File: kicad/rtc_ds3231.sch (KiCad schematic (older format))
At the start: 10 parts, among them U6 DS3231N

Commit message: footprint corrections on PCB
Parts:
- BT1: symbol KlokTHREEjr:Batt_RTC -> wyostat:Batt_RTC; manf# (none) -> mfr_pn
- C8: symbol KlokTHREEjr:C_NP -> wyostat:C_NP; manf# (none) -> mfr_pn
- R26, R27, R28, R29: symbol KlokTHREEjr:R -> wyostat:R; manf# (none) -> mfr_pn
- TP1, TP2, TP3: symbol KlokTHREEjr:Conn_01x01 -> wyostat:Conn_01x01; manf# (none) -> mfr_pn
- U6: symbol KlokTHREEjr:DS3231N -> wyostat:DS3231N; manf# (none) -> mfr_pn
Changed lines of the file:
@@
 $EndDescr
 $Comp
-L KlokTHREEjr:R R28
+L wyostat:R R28
 U 1 1 5A448924
 P 2525 2750
@@
 F 2 "wyostat_fp:R_0805" V 2455 2750 30  0001 C CNN
 F 3 "~" H 2525 2750 30  0000 C CNN
+F 4 "mfr_pn" H 2525 2750 50  0001 C CNN "manf#"
 	1    2525 2750
 	1    0    0    -1
 $EndComp
 $Comp
-L KlokTHREEjr:GND #PWR017
+L wyostat:GND #PWR017
 U 1 1 5A44892B
 P 3675 4175
@@
 F 2 "" H 3675 4175 60  0000 C CNN
 F 3 "" H 3675 4175 60  0000 C CNN
+F 4 "mfr_pn" H 3675 4175 50  0001 C CNN "manf#"
 	1    3675 4175
 	1    0    0    -1
 $EndComp
 $Comp
-L KlokTHREEjr:R R26
+L wyostat:R R26
 U 1 1 5A448933
 P 4900 2550
@@
 F 2 "wyostat_fp:R_0805" V 4830 2550 30  0001 C CNN
 F 3 "~" H 4900 2550 30  0000 C CNN
+F 4 "mfr_pn" H 4900 2550 50  0001 C CNN "manf#"
 	1    4900 2550
 	1    0    0    -1
 $EndComp
 $Comp
-L KlokTHREEjr:R R27
+L wyostat:R R27
 U 1 1 5A44893A
 P 5050 2550
@@
 F 2 "wyostat_fp:R_0805" V 4980 2550 30  0001 C CNN
 F 3 "~" H 5050 2550 30  0000 C CNN
+F 4 "mfr_pn" H 5050 2550 50  0001 C CNN "manf#"
 	1    5050 2550
 	1    0    0    -1
@@
 RESET
 $Comp
-L KlokTHREEjr:PWR_FLAG #FLG018
+L wyostat:PWR_FLAG #FLG018
 U 1 1 5A448942
 P 2000 2325
@@
 F 2 "" H 2000 2325 60  0000 C CNN
 F 3 "" H 2000 2325 60  0000 C CNN
+F 4 "mfr_pn" H 2000 2325 50  0001 C CNN "manf#"
 	1    2000 2325
 	1    0    0    -1
 $EndComp
 $Comp
-L KlokTHREEjr:DS3231N U6
+L wyostat:DS3231N U6
 U 1 1 5A448948
 P 3675 3200
@@
 F 2 "wyostat_fp:DS3231" H 3675 3200 60  0001 C CNN
 F 3 "~" H 3675 3200 60  0000 C CNN
+F 4 "mfr_pn" H 3675 3200 50  0001 C CNN "manf#"
 	1    3675 3200
 	1    0    0    -1
 $EndComp
 $Comp
-L KlokTHREEjr:R R29
+L wyostat:R R29
 U 1 1 5A44894F
 P 2675 2750
@@
 F 2 "wyostat_fp:R_0805" V 2605 2750 30  0001 C CNN
 F 3 "~" H 2675 2750 30  0000 C CNN
+F 4 "mfr_pn" H 2675 2750 50  0001 C CNN "manf#"
 	1    2675 2750
 	1    0    0    -1
 $EndComp
 $Comp
-L KlokTHREEjr:Batt_RTC BT1
+L wyostat:Batt_RTC BT1
 U 1 1 5A448957
 P 2000 3200
@@
 F 2 "wyostat_fp:CR2032_SMD2" H 2000 3200 60  0001 C CNN
 F 3 "" H 2000 3200 60  0000 C CNN
-F 4 "BU2032SM-HD-GCT-ND " H 2100 3500 60  0001 C CNN "Digikey"
+F 4 "mfr_pn" H 2000 3200 50  0001 C CNN "manf#"
+F 5 "BU2032SM-HD-GCT-ND " H 2100 3500 60  0001 C CNN "Digikey"
 	1    2000 3200
 	0    1    1    0
@@
 SCL
 $Comp
-L KlokTHREEjr:C_NP C8
+L wyostat:C_NP C8
 U 1 1 5A613CC0
 P 2200 3175
@@
 F 2 "wyostat_fp:C_0805" H 2200 3175 60  0001 C CNN
 F 3 "" H 2200 3175 60  0000 C CNN
+F 4 "mfr_pn" H 2200 3175 50  0001 C CNN "manf#"
 	1    2200 3175
 	1    0    0    -1
@@
 	4625 4100 7775 4100
 $Comp
-L KlokTHREEjr:Conn_01x01 TP1
+L wyostat:Conn_01x01 TP1
 U 1 1 5A48EA43
 P 7750 3000
@@
 F 2 "wyostat_fp:Pin_Header_Straight_1x01" H 7750 3000 50  0001 C CNN
 F 3 "~" H 7750 3000 50  0001 C CNN
+F 4 "mfr_pn" H 7750 3000 50  0001 C CNN "manf#"
 	1    7750 3000
 	1    0    0    -1
@@
 SCL
 $Comp
-L KlokTHREEjr:Conn_01x01 TP2
+L wyostat:Conn_01x01 TP2
 U 1 1 5A95B66E
 P 7750 2850
@@
 F 2 "wyostat_fp:Pin_Header_Straight_1x01" H 7750 2850 50  0001 C CNN
 F 3 "~" H 7750 2850 50  0001 C CNN
+F 4 "mfr_pn" H 7750 2850 50  0001 C CNN "manf#"
 	1    7750 2850
 	1    0    0    -1
 $EndComp
 $Comp
-L KlokTHREEjr:Conn_01x01 TP3
+L wyostat:Conn_01x01 TP3
 U 1 1 5A95B721
 P 7750 3150
@@
 F 2 "wyostat_fp:Pin_Header_Straight_1x01" H 7750 3150 50  0001 C CNN
 F 3 "~" H 7750 3150 50  0001 C CNN
+F 4 "mfr_pn" H 7750 3150 50  0001 C CNN "manf#"
 	1    7750 3150
 	1    0    0    -1

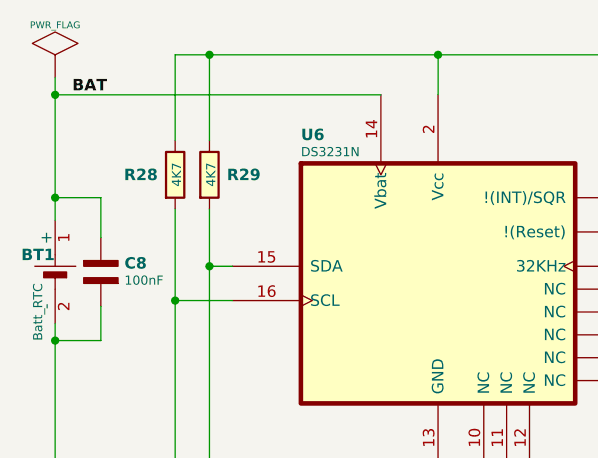
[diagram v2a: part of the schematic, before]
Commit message: prettified silk legend
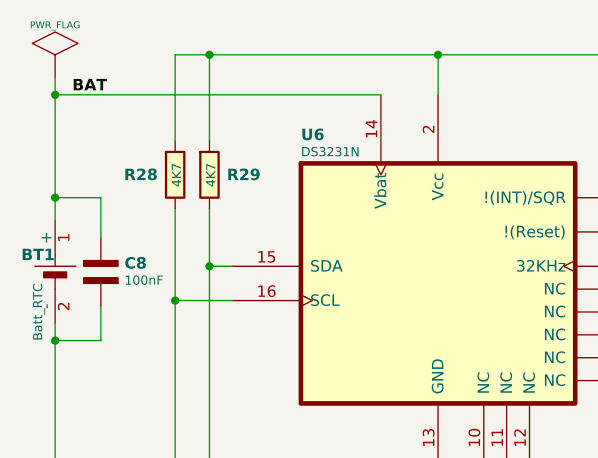
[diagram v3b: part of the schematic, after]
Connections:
- net 3V3: now also R28.2, R29.2; no longer R28.1, R29.1
- net SCL: now also R28.1; no longer R28.2
- net SDA: now also R29.1; no longer R29.2
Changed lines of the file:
@@
 F 4 "mfr_pn" H 2525 2750 50  0001 C CNN "manf#"
 	1    2525 2750
-	1    0    0    -1
+	1    0    0    1
 $EndComp
 $Comp
-L wyostat:GND #PWR017
+L wyostat:GND #PWR?
 U 1 1 5A44892B
 P 3675 4175
-F 0 "#PWR017" H 3675 4175 30  0001 C CNN
+F 0 "#PWR?" H 3675 4175 30  0001 C CNN
 F 1 "GND" H 3675 4105 30  0001 C CNN
 F 2 "" H 3675 4175 60  0000 C CNN
@@
 RESET
 $Comp
-L wyostat:PWR_FLAG #FLG018
+L wyostat:PWR_FLAG #FLG?
 U 1 1 5A448942
 P 2000 2325
-F 0 "#FLG018" H 2000 2595 30  0001 C CNN
+F 0 "#FLG?" H 2000 2595 30  0001 C CNN
 F 1 "PWR_FLAG" H 2000 2555 30  0000 C CNN
 F 2 "" H 2000 2325 60  0000 C CNN
@@
 F 4 "mfr_pn" H 2675 2750 50  0001 C CNN "manf#"
 	1    2675 2750
-	1    0    0    -1
+	1    0    0    1
 $EndComp
 $Comp
